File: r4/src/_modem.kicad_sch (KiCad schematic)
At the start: 50 parts, among them J1 , J11 SMA, J12 U_FL-R-SMT-1_10_, J13 JAE_SIM_Card_SF72S006, J2 , J3 , J4 , J5 , J6 , J7 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

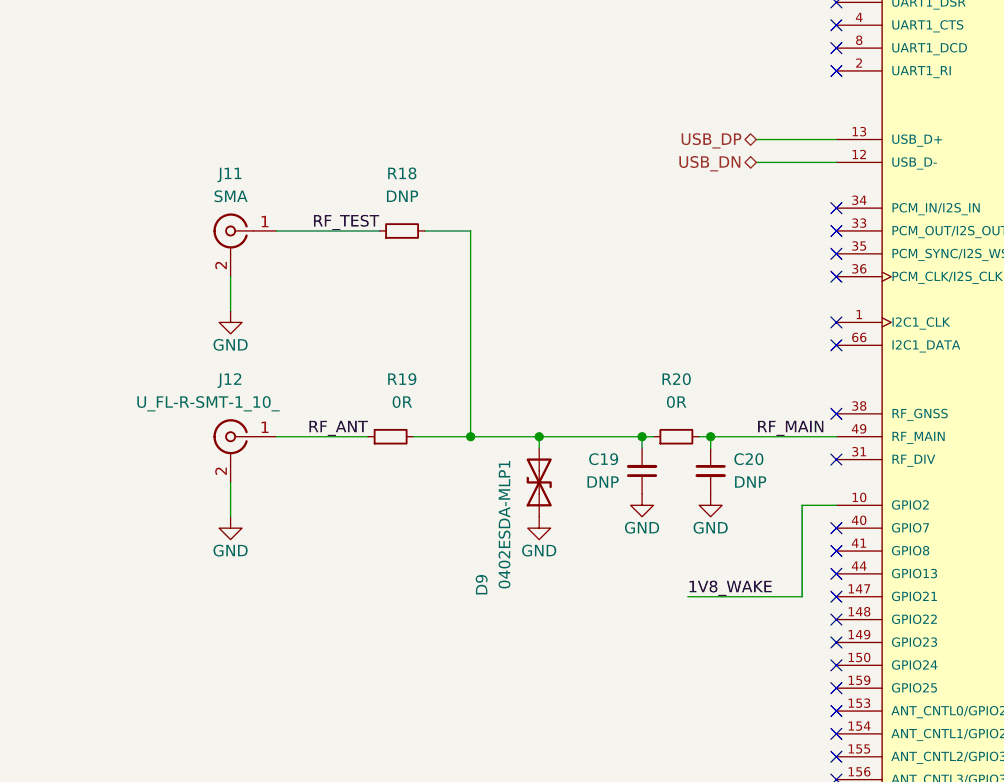
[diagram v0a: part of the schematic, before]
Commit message: Add antenna diversity connector, remove SMA. Parts will be DNP in this revision
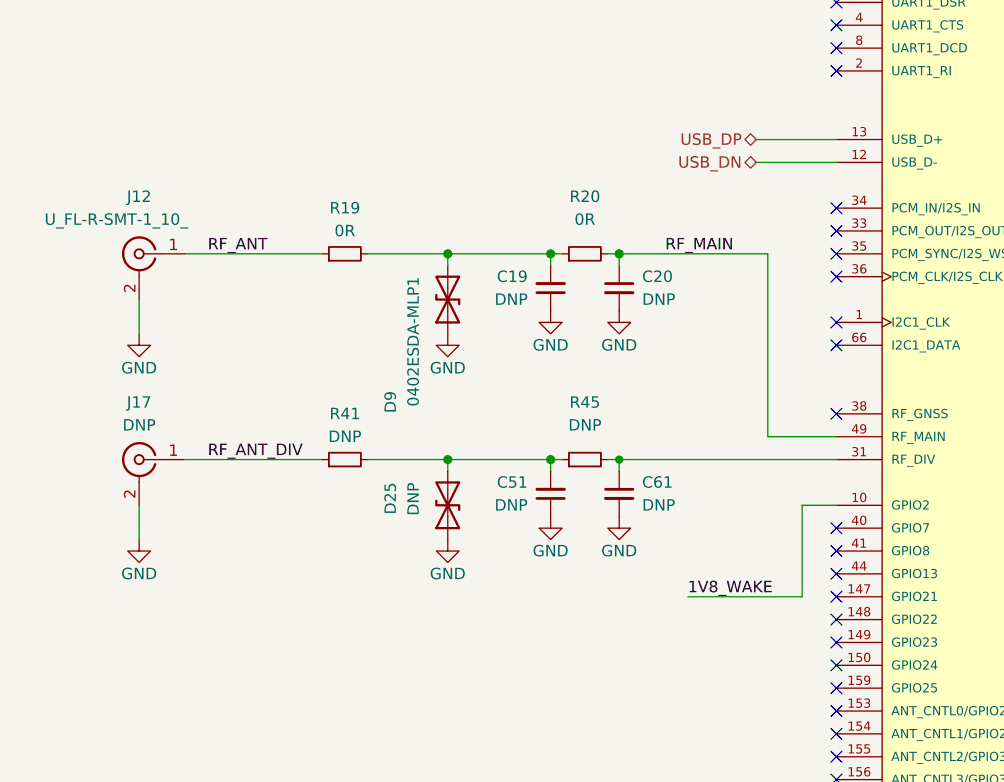
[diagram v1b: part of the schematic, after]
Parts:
- removed J11: SMA, Connector_Coaxial:SMA_Amphenol_132134-10_Vertical, symbol Connector:Conn_Coaxial
- removed R18: DNP, Resistor_SMD:R_0402_1005Metric, symbol Device:R_Small
- added C51, C61: DNP, Capacitor_SMD:C_0402_1005Metric, symbol Device:C_Small
- added D25: DNP, Diode_SMD:D_0402_1005Metric, symbol Device:D_TVS
- added J17: DNP, Connector_Coaxial:U.FL_Hirose_U.FL-R-SMT-1_Vertical, symbol Connector:Conn_Coaxial
- added R41, R45: DNP, Resistor_SMD:R_0402_1005Metric, symbol Device:R_Small
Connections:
- net GND: now also U8.8, C51.1, C61.2, D25.1 (A1), J17.2 (Ext)
- net UIM_CLK_R: now also U8.7
- net UIM_DATA: now also U8.6
- net UIM_RESET_N: now also U8.9
- net UIM_VCC: now also U8.10
- net at U7.31 (RF_DIV): now also C61.1, R45.2
- new net: C51.2, D25.2 (A2), R41.2, R45.1
- new net RF_ANT_DIV: J17.1 (In), R41.1
- no-connect marks 49 -> 48
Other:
- moved on the sheet: C19, C20, D9, J12, R19, R20

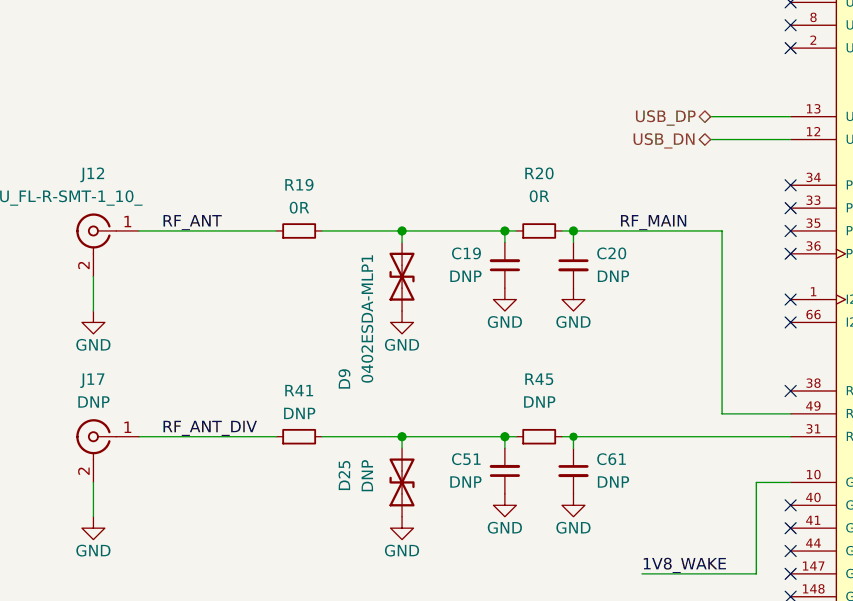
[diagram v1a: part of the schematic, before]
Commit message: Lay out antenna sections with correct width and clearance calculated as coplanar waveguides. Stackup documented in the /build folder.
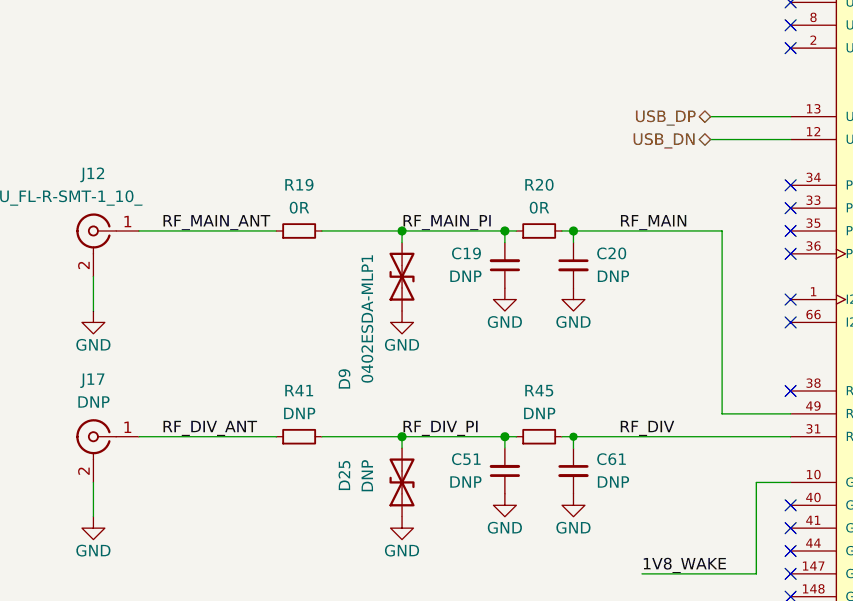
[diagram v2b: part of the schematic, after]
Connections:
- net RF_DIV: now reaches C61.1, R45.2, U7.31 (RF_DIV)
- net RF_DIV_PI: now reaches C51.2, D25.2 (A2), R41.2, R45.1
- net RF_MAIN_PI: now reaches C19.2, D9.2 (A2), R19.2, R20.1
- net RF_ANT renamed RF_MAIN_ANT
- net RF_ANT_DIV renamed RF_DIV_ANT
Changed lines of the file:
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@@
     (effects (font (size 1.27 1.27)) (justify right bottom))
+  )
+  (label "RF_DIV" (at 90.17 156.21 0) (fields_autoplaced)
+    (effects (font (size 1.27 1.27)) (justify left bottom))
   )
   (label "1V8_TX_ON" (at 199.39 143.51 180) (fields_autoplaced)
@@
     (effects (font (size 1.27 1.27)) (justify left bottom))
   )
-  (label "RF_ANT" (at 39.37 133.35 0) (fields_autoplaced)
+  (label "RF_MAIN_ANT" (at 39.37 133.35 0) (fields_autoplaced)
     (effects (font (size 1.27 1.27)) (justify left bottom))
   )
@@
     (effects (font (size 1.27 1.27)) (justify right bottom))
   )
-  (label "RF_ANT_DIV" (at 39.37 156.21 0) (fields_autoplaced)
+  (label "RF_DIV_ANT" (at 39.37 156.21 0) (fields_autoplaced)
     (effects (font (size 1.27 1.27)) (justify left bottom))
   )
@@
     (effects (font (size 1.27 1.27)) (justify left bottom))
   )
+  (label "RF_MAIN_PI" (at 66.04 133.35 0) (fields_autoplaced)
+    (effects (font (size 1.27 1.27)) (justify left bottom))
+  )
   (label "1V8_POWER_ON_N" (at 88.9 66.04 0) (fields_autoplaced)
     (effects (font (size 1.27 1.27)) (justify left bottom))
@@
   )
   (label "1V8_WAKE" (at 92.71 171.45 0) (fields_autoplaced)
+    (effects (font (size 1.27 1.27)) (justify left bottom))
+  )
+  (label "RF_DIV_PI" (at 66.04 156.21 0) (fields_autoplaced)
     (effects (font (size 1.27 1.27)) (justify left bottom))
   )
@@
   (symbol (lib_id "Device:R_Small") (at 81.28 156.21 90) (unit 1)
     (in_bom yes) (on_board yes) (dnp no)
-    (property "Reference" "R45" (at 81.28 149.86 90)
-      (effects (font (size 1.27 1.27)))
-    )
-    (property "Value" "DNP" (at 81.28 152.4 90)
+    (property "Reference" "R45" (at 81.28 151.13 90)
+      (effects (font (size 1.27 1.27)))
+    )
+    (property "Value" "DNP" (at 81.28 153.67 90)
       (effects (font (size 1.27 1.27)))
     )
@@
   (symbol (lib_id "Device:R_Small") (at 81.28 133.35 90) (unit 1)
     (in_bom yes) (on_board yes) (dnp no)
-    (property "Reference" "R20" (at 81.28 127 90)
-      (effects (font (size 1.27 1.27)))
-    )
-    (property "Value" "0R" (at 81.28 129.54 90)
-      (effects (font (size 1.27 1.27)))
-    )
+    (property "Reference" "R20" (at 81.28 128.27 90)
+      (effects (font (size 1.27 1.27)))
+    )
+    (property "Value" "0R" (at 81.28 130.81 90)
+      (effects (font (size 1.27 1.27)))
+    )

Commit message: ERC pass. A few errors remain but they are impossible to fix.
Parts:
- C26: footprint Capacitor_SMD:C_0603_1608Metric -> Capacitor_SMD:C_0402_1005Metric
- C28: value 1nF -> 10nF; footprint Capacitor_SMD:C_0603_1608Metric -> Capacitor_SMD:C_0402_1005Metric; Voltage (none) -> 50V
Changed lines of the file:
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@@
     (pin "98")
     (pin "99")
+    (pin "100")
+    (pin "102")
+    (pin "103")
+    (pin "107")
+    (pin "108")
+    (pin "114")
+    (pin "115")
+    (pin "116")
+    (pin "117")
+    (pin "118")
+    (pin "119")
+    (pin "120")
+    (pin "121")
+    (pin "122")
+    (pin "123")
+    (pin "124")
+    (pin "129")
+    (pin "130")
+    (pin "131")
+    (pin "132")
+    (pin "133")
+    (pin "134")
+    (pin "135")
+    (pin "14")
+    (pin "140")
+    (pin "141")
+    (pin "142")
+    (pin "143")
+    (pin "144")
+    (pin "145")
+    (pin "146")
+    (pin "15")
+    (pin "160")
+    (pin "161")
+    (pin "162")
+    (pin "163")
+    (pin "164")
+    (pin "165")
+    (pin "166")
+    (pin "17")
+    (pin "18")
+    (pin "19")
+    (pin "20")
+    (pin "21")
+    (pin "55")
+    (pin "56")
+    (pin "57")
+    (pin "58")
+    (pin "71")
+    (pin "72")
+    (pin "73")
+    (pin "74")
+    (pin "75")
+    (pin "76")
+    (pin "77")
+    (pin "78")
+    (pin "79")
+    (pin "80")
+    (pin "81")
+    (pin "82")
+    (pin "83")
+    (pin "84")
+    (pin "85")
+    (pin "86")
+    (pin "87")
+    (pin "88")
+    (pin "89")
+    (pin "90")
+    (pin "91")
+    (pin "92")
+    (pin "93")
+    (pin "94")
+    (pin "95")
     (pin "43")
     (instances
@@
       (effects (font (size 1.27 1.27)) (justify left))
     )
-    (property "Footprint" "Capacitor_SMD:C_0603_1608Metric" (at 317.5 69.85 0)
+    (property "Footprint" "Capacitor_SMD:C_0402_1005Metric" (at 317.5 69.85 0)
       (effects (font (size 1.27 1.27)) hide)
     )
@@
       (project "bugg-main-r4"
         (path "/e3eb514f-6ce4-4abe-ba20-f82f0015628f/c8d4c890-e18c-4f0d-b5c7-f5d98c418551"
-          (reference "C26") (unit 1) (value "100nF") (footprint "Capacitor_SMD:C_0603_1608Metric")
+          (reference "C26") (unit 1) (value "100nF") (footprint "Capacitor_SMD:C_0402_1005Metric")
         )
       )
@@
       (effects (font (size 1.27 1.27)) (justify left))
     )
-    (property "Value" "1nF" (at 331.47 71.12 0)
-      (effects (font (size 1.27 1.27)) (justify left))
-    )
-    (property "Footprint" "Capacitor_SMD:C_0603_1608Metric" (at 328.93 69.85 0)
+    (property "Value" "10nF" (at 331.47 71.12 0)
+      (effects (font (size 1.27 1.27)) (justify left))
+    )
+    (property "Footprint" "Capacitor_SMD:C_0402_1005Metric" (at 328.93 69.85 0)
       (effects (font (size 1.27 1.27)) hide)
     )
@@
       (effects (font (size 1.27 1.27)) hide)
     )
-    (pin "1")
-    (pin "2")
-    (instances
-      (project "bugg-main-r4"
-        (path "/e3eb514f-6ce4-4abe-ba20-f82f0015628f/c8d4c890-e18c-4f0d-b5c7-f5d98c418551"
-          (reference "C28") (unit 1) (value "1nF") (footprint "Capacitor_SMD:C_0603_1608Metric")
-        )
-      )
+    (property "Voltage" "50V" (at 328.93 69.85 0)
+      (effects (font (size 1.27 1.27)) hide)
+    )
+    (pin "1")
+    (pin "2")
+    (instances
+      (project "bugg-main-r4"
+        (path "/e3eb514f-6ce4-4abe-ba20-f82f0015628f/c8d4c890-e18c-4f0d-b5c7-f5d98c418551"
+          (reference "C28") (unit 1) (value "10nF") (footprint "Capacitor_SMD:C_0402_1005Metric")
+        )
+      )

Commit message: Change some passive values and packages to get rid of some BOM lines
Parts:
- C28: Tempco (none) -> NP0
- R21, R22, R23: footprint Resistor_SMD:R_0603_1608Metric -> Resistor_SMD:R_0402_1005Metric
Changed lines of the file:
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@@
       (effects (font (size 1.27 1.27)))
     )
-    (property "Footprint" "Resistor_SMD:R_0603_1608Metric" (at 285.75 82.55 0)
+    (property "Footprint" "Resistor_SMD:R_0402_1005Metric" (at 285.75 82.55 0)
       (effects (font (size 1.27 1.27)) hide)
     )
@@
       (project "bugg-main-r4"
         (path "/e3eb514f-6ce4-4abe-ba20-f82f0015628f/c8d4c890-e18c-4f0d-b5c7-f5d98c418551"
-          (reference "R23") (unit 1) (value "0R") (footprint "Resistor_SMD:R_0603_1608Metric")
+          (reference "R23") (unit 1) (value "0R") (footprint "Resistor_SMD:R_0402_1005Metric")
         )
       )
@@
       (effects (font (size 1.27 1.27)) (justify right))
     )
-    (property "Footprint" "Resistor_SMD:R_0603_1608Metric" (at 280.67 72.39 0)
+    (property "Footprint" "Resistor_SMD:R_0402_1005Metric" (at 280.67 72.39 0)
       (effects (font (size 1.27 1.27)) hide)
     )
@@
       (project "bugg-main-r4"
         (path "/e3eb514f-6ce4-4abe-ba20-f82f0015628f/c8d4c890-e18c-4f0d-b5c7-f5d98c418551"
-          (reference "R22") (unit 1) (value "DNP 15k") (footprint "Resistor_SMD:R_0603_1608Metric")
+          (reference "R22") (unit 1) (value "DNP 15k") (footprint "Resistor_SMD:R_0402_1005Metric")
         )
       )
@@
       (effects (font (size 1.27 1.27)) (justify right))
     )
-    (property "Footprint" "Resistor_SMD:R_0603_1608Metric" (at 267.97 72.39 0)
+    (property "Footprint" "Resistor_SMD:R_0402_1005Metric" (at 267.97 72.39 0)
       (effects (font (size 1.27 1.27)) hide)
     )
@@
       (project "bugg-main-r4"
         (path "/e3eb514f-6ce4-4abe-ba20-f82f0015628f/c8d4c890-e18c-4f0d-b5c7-f5d98c418551"
-          (reference "R21") (unit 1) (value "10k") (footprint "Resistor_SMD:R_0603_1608Metric")
+          (reference "R21") (unit 1) (value "10k") (footprint "Resistor_SMD:R_0402_1005Metric")
         )
       )
@@
       (effects (font (size 1.27 1.27)) hide)
     )
+    (property "Tempco" "NP0" (at 328.93 69.85 0)
+      (effects (font (size 1.27 1.27)) hide)
+    )

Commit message: Create new UFL footprint with keepout. Add it to the layout
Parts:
- J12, J17: footprint Connector_Coaxial:U.FL_Hirose_U.FL-R-SMT-1_Vertical -> jeffmakes-footprints:U.FL_Hirose_U.FL-R-SMT-1-copper-keepout
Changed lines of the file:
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@@
       (effects (font (size 1.27 1.27)))
     )
-    (property "Footprint" "Connector_Coaxial:U.FL_Hirose_U.FL-R-SMT-1_Vertical" (at 31.75 156.21 0)
+    (property "Footprint" "jeffmakes-footprints:U.FL_Hirose_U.FL-R-SMT-1-copper-keepout" (at 31.75 156.21 0)
       (effects (font (size 1.27 1.27)) hide)
     )
@@
       (project "bugg-main-r4"
         (path "/e3eb514f-6ce4-4abe-ba20-f82f0015628f/c8d4c890-e18c-4f0d-b5c7-f5d98c418551"
-          (reference "J17") (unit 1) (value "DNP") (footprint "Connector_Coaxial:U.FL_Hirose_U.FL-R-SMT-1_Vertical")
+          (reference "J17") (unit 1) (value "DNP") (footprint "jeffmakes-footprints:U.FL_Hirose_U.FL-R-SMT-1-copper-keepout")
         )
       )
@@
       (effects (font (size 1.27 1.27)))
     )
-    (property "Footprint" "Connector_Coaxial:U.FL_Hirose_U.FL-R-SMT-1_Vertical" (at 31.75 133.35 0)
+    (property "Footprint" "jeffmakes-footprints:U.FL_Hirose_U.FL-R-SMT-1-copper-keepout" (at 31.75 133.35 0)
       (effects (font (size 1.27 1.27)) hide)
     )
@@
       (project "bugg-main-r4"
         (path "/e3eb514f-6ce4-4abe-ba20-f82f0015628f/c8d4c890-e18c-4f0d-b5c7-f5d98c418551"
-          (reference "J12") (unit 1) (value "U_FL-R-SMT-1_10_") (footprint "Connector_Coaxial:U.FL_Hirose_U.FL-R-SMT-1_Vertical")
-        )
-      )
+          (reference "J12") (unit 1) (value "U_FL-R-SMT-1_10_") (footprint "jeffmakes-footprints:U.FL_Hirose_U.FL-R-SMT-1-copper-keepout")
+        )
+      )

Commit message: Remove NP0 constraint from 10nF 50V caps. The only instance that could have demanded NP0 is the 15V DCDC,  ut its eval board BOM uses X7R's.
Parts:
- C28: Tempco NP0 -> (none)
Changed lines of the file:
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@@
-      (effects (font (size 1.27 1.27)) hide)
-    )
-    (property "Tempco" "NP0" (at 328.93 69.85 0)
       (effects (font (size 1.27 1.27)) hide)
     )
